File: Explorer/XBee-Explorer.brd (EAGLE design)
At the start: 35.6 x 27.9 mm, 31 parts, among them U2 XBEE-1B3, U3 MIC5205 3.3V, U4 FT231XS, X1 USBSMD

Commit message: Added jumper to disconnect RSSI LED, moved silk
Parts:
- removed U$2: CREATIVE_COMMONS, SparkFun:CREATIVE_COMMONS
- added FRAME1: FRAME-LETTER, SparkFun-Aesthetics:CREATIVE_COMMONS
- added LOGO1: OSHW-LOGOS, SparkFun-Aesthetics:OSHW-LOGO-S
- added SJ1: RSSI_LED_EN, SparkFun-Passives:SJ_2S-TRACE
- JP5, JP6: value M11PTH -> M111X11_NO_SILK; device SparkFun-Connectors:1X11 -> SparkFun-Connectors:1X11_NO_SILK
- moved JP4 1.80 mm to (3.81, 26.7)
- moved JP1 0.36 mm to (31.8, 1.27)
- moved U$1 0.13 mm to (4.70, 1.27)
- turned LED2 to 180 degrees
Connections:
- new net N$9: R7.2, SJ1.2
- net RSSI: now also SJ1.1; no longer R7.2
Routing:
- net N$9: track 0.00 -> 5.75 mm, vias 0 -> 1
- net TXLED: track 19.5 -> 20.3 mm
- net N$1: track 6.66 -> 7.28 mm
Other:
- board text added: "Nathan Seidle, Jim Lindblom"
- board text added: "RSSI LED"
- board text added: "v21"
- board text removed: "v20"
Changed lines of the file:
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@@
 <?xml version="1.0" encoding="utf-8"?>
 <!DOCTYPE eagle SYSTEM "eagle.dtd">
-<eagle version="6.4">
+<eagle version="6.5.0">
 <drawing>
 <settings>
@@
 <layer number="106" name="bPlate" color="7" fill="1" visible="no" active="yes"/>
 <layer number="107" name="Crop" color="7" fill="1" visible="no" active="yes"/>
+<layer number="108" name="tplace-old" color="10" fill="1" visible="no" active="yes"/>
+<layer number="109" name="ref-old" color="11" fill="1" visible="no" active="yes"/>
 <layer number="116" name="Patch_BOT" color="9" fill="4" visible="no" active="yes"/>
 <layer number="121" name="_tsilk" color="7" fill="1" visible="no" active="yes"/>
@@
 <wire x1="27.686" y1="1.778" x2="33.401" y2="8.382" width="0.254" layer="21"/>
 <wire x1="27.686" y1="26.162" x2="33.401" y2="19.558" width="0.254" layer="21"/>
-<text x="0.762" y="21.082" size="1.016" layer="21" ratio="15">PWR</text>
-<text x="31.796" y="13.413" size="1.016" layer="21" ratio="15">TX</text>
-<text x="31.877" y="9.652" size="1.016" layer="21" ratio="15">RX</text>
-<text x="1.27" y="12.446" size="1.27" layer="16" ratio="20" rot="MR90">v20</text>
-<text x="30.353" y="17.272" size="1.016" layer="21" ratio="15">RSSI</text>
+<text x="2.54" y="21.082" size="1.016" layer="21" ratio="15" align="bottom-center">PWR</text>
+<text x="33.655" y="13.97" size="1.016" layer="21" ratio="15" align="center-right">TX</text>
+<text x="33.655" y="10.16" size="1.016" layer="21" ratio="15" align="center-right">RX</text>
+<text x="1.27" y="12.446" size="1.27" layer="16" ratio="20" rot="MR90">v21</text>
+<text x="33.655" y="17.78" size="1.016" layer="21" ratio="15" align="center-right">RSSI</text>
 <text x="28.448" y="20.066" size="1.016" layer="22" ratio="15" rot="MR270">3.3V</text>
 <text x="25.908" y="20.066" size="1.016" layer="22" ratio="15" rot="MR270">DOUT</text>
@@
 <text x="4.572" y="7.874" size="1.016" layer="22" ratio="15" rot="MR90">5V</text>
 <text x="30.988" y="20.066" size="1.016" layer="22" ratio="15" rot="MR270">GND</text>
-<text x="21.59" y="-7.62" size="1.778" layer="21" font="vector" ratio="15">N. Seidle</text>
+<text x="21.59" y="-7.62" size="1.778" layer="27" font="vector" ratio="15">N. Seidle</text>
+<wire x1="14.732" y1="24.13" x2="15.748" y2="24.13" width="0.4064" layer="30"/>
+<text x="15.24" y="25.908" size="0.889" layer="22" ratio="15" rot="MR0" align="center">RSSI LED</text>
+<text x="17.78" y="-10.16" size="1.778" layer="51" font="vector">Nathan Seidle, Jim Lindblom</text>
 </plain>
 <attributes>
@@
 <attribute name="VALUE" x="3.937" y="19.6215" size="0.4064" layer="27"/>
 </element>
-<element name="LED2" library="SparkFun" package="LED-0603" value="Red-TX" x="34.29" y="13.97" smashed="yes">
-<attribute name="NAME" x="34.29" y="11.97" size="1.27" layer="25" rot="R270"/>
-<attribute name="VALUE" x="34.925" y="13.398" size="0.4064" layer="27" rot="R270"/>
+<element name="LED2" library="SparkFun" package="LED-0603" value="Red-TX" x="34.29" y="13.97" smashed="yes" rot="R180">
+<attribute name="NAME" x="34.29" y="15.97" size="1.27" layer="25" rot="R90"/>
+<attribute name="VALUE" x="33.655" y="14.542" size="0.4064" layer="27" rot="R90"/>
 </element>
 <element name="LED3" library="SparkFun" package="LED-0603" value="Green-RX" x="34.29" y="10.16" smashed="yes" rot="R180">
@@
 <attribute name="VALUE" x="33.528" y="10.732" size="0.4064" layer="27" rot="R90"/>
 </element>
-<element name="U$1" library="SparkFun" package="SFE-LOGO-FLAME" value="LOGO-SFESK" x="4.826" y="1.27"/>
+<element name="U$1" library="SparkFun" package="SFE-LOGO-FLAME" value="LOGO-SFESK" x="4.699" y="1.27"/>
 <element name="U$4" library="SparkFun" package="SFE-NEW-WEBLOGO" value="LOGO-SFENEW" x="26.924" y="11.43" rot="MR0"/>
 <element name="U2" library="SparkFun" package="XBEE-SMD" value="XBEE-1B3" x="6.35" y="13.97" smashed="yes" rot="R270">
@@
 <element name="U3" library="SparkFun" package="SOT23-5" value="MIC5205 3.3V" x="27.94" y="17.78" rot="R270"/>
 <element name="C1" library="SparkFun" package="EIA3216" value="10uF" x="27.94" y="12.7"/>
-<element name="U$2" library="SparkFun" package="CREATIVE_COMMONS" value="CREATIVE_COMMONS" x="-10.16" y="-7.62"/>
-<element name="JP1" library="SparkFun" package="MICRO-FIDUCIAL" value="FIDUCIALUFIDUCIAL" x="31.496" y="1.016"/>
-<element name="JP4" library="SparkFun" package="MICRO-FIDUCIAL" value="FIDUCIALUFIDUCIAL" x="5.08" y="25.4"/>
+<element name="JP1" library="SparkFun" package="MICRO-FIDUCIAL" value="FIDUCIALUFIDUCIAL" x="31.75" y="1.27"/>
+<element name="JP4" library="SparkFun" package="MICRO-FIDUCIAL" value="FIDUCIALUFIDUCIAL" x="3.81" y="26.67"/>
 <element name="U4" library="SparkFun-DigitalIC" package="SSOP20_L" value="FT231XS" x="19.05" y="13.97" rot="R180"/>
 <element name="R2" library="SparkFun-Resistors" package="0603-RES" value="27" x="11.43" y="14.224"/>
@@
 <element name="C6" library="SparkFun-Capacitors" package="0603-CAP" value="0.1uF" x="15.24" y="8.89" rot="R180"/>
 <element name="C7" library="SparkFun-Capacitors" package="0603-CAP" value="0.1uF" x="27.94" y="15.24" rot="R180"/>
-<element name="JP5" library="SparkFun-Connectors" package="1X11" value="M11PTH" x="5.08" y="21.463"/>
-<element name="JP6" library="SparkFun-Connectors" package="1X11" value="M11PTH" x="30.48" y="6.477" rot="R180"/>
+<element name="JP5" library="SparkFun-Connectors" package="1X11_NO_SILK" value="M111X11_NO_SILK" x="5.08" y="21.463"/>
+<element name="JP6" library="SparkFun-Connectors" package="1X11_NO_SILK" value="M111X11_NO_SILK" x="30.48" y="6.477" rot="R180"/>
+<element name="SJ1" library="SparkFun-Passives" package="SJ_2S-TRACE" value="RSSI_LED_EN" x="15.24" y="24.13" rot="MR180"/>
+<element name="FRAME1" library="SparkFun-Aesthetics" package="CREATIVE_COMMONS" value="FRAME-LETTER" x="-12.7" y="-10.16"/>
+<element name="LOGO1" library="SparkFun-Aesthetics" package="OSHW-LOGO-S" value="OSHW-LOGOS" x="5.588" y="25.908" rot="R90"/>
 </elements>
 <signals>
@@
 <contactref element="LED2" pad="A"/>
 <contactref element="R4" pad="2"/>
-<wire x1="28.79" y1="10.414" x2="30.734" y2="10.414" width="0.254" layer="1"/>
-<wire x1="34.29" y1="13.22" x2="33.54" y2="13.22" width="0.254" layer="1"/>
-<wire x1="33.54" y1="13.22" x2="30.734" y2="10.414" width="0.254" layer="1"/>
+<wire x1="28.79" y1="10.414" x2="29.337" y2="10.414" width="0.254" layer="1"/>
+<wire x1="33.643" y1="14.72" x2="29.337" y2="10.414" width="0.254" layer="1"/>
+<wire x1="34.29" y1="14.72" x2="33.643" y2="14.72" width="0.254" layer="1"/>
 </signal>
 <signal name="N$4">
@@
 <contactref element="U4" pad="10"/>
 <via x="17.7165" y="15.3035" extent="1-16" drill="0.508"/>
-<wire x1="17.7165" y1="15.3035" x2="31.6865" y2="15.3035" width="0.254" layer="16"/>
+<wire x1="17.7165" y1="15.3035" x2="30.7975" y2="15.3035" width="0.254" layer="16"/>
 <wire x1="16.1925" y1="16.6497" x2="16.1925" y2="15.6845" width="0.254" layer="1"/>
 <wire x1="16.1925" y1="15.6845" x2="16.5735" y2="15.3035" width="0.254" layer="1"/>
 <wire x1="17.7165" y1="15.3035" x2="16.5735" y2="15.3035" width="0.254" layer="1"/>
-<wire x1="31.6865" y1="15.3035" x2="31.75" y2="15.24" width="0.254" layer="16"/>
-<via x="31.75" y="15.24" extent="1-16" drill="0.508"/>
-<wire x1="31.75" y1="15.24" x2="32.27" y2="14.72" width="0.254" layer="1"/>
-<wire x1="32.27" y1="14.72" x2="34.29" y2="14.72" width="0.254" layer="1"/>
+<wire x1="34.29" y1="13.22" x2="33.413" y2="13.22" width="0.254" layer="1"/>
+<wire x1="33.413" y1="13.22" x2="33.147" y2="12.954" width="0.254" layer="1"/>
+<via x="33.147" y="12.954" extent="1-16" drill="0.508"/>
+<wire x1="33.147" y1="12.954" x2="30.7975" y2="15.3035" width="0.254" layer="16"/>
 </signal>
 <signal name="DIO4">
@@
 <wire x1="10.35" y1="26.47" x2="10.35" y2="23.685" width="0.254" layer="1"/>
 <via x="21.6535" y="18.288" extent="1-16" drill="0.508"/>
-<wire x1="19.7485" y1="20.193" x2="8.89" y2="20.193" width="0.254" layer="16"/>
-<wire x1="8.89" y1="20.193" x2="7.62" y2="21.463" width="0.254" layer="16"/>
-<wire x1="19.7485" y1="20.193" x2="21.6535" y2="18.288" width="0.254" layer="16"/>
+<wire x1="10.033" y1="19.05" x2="7.62" y2="21.463" width="0.254" layer="16"/>
 <wire x1="21.9075" y1="16.6497" x2="21.9075" y2="18.034" width="0.254" layer="1"/>
 <wire x1="21.9075" y1="18.034" x2="21.6535" y2="18.288" width="0.254" layer="1"/>
 <contactref element="JP5" pad="2"/>
+<wire x1="21.6535" y1="18.288" x2="20.8915" y2="19.05" width="0.254" layer="16"/>
+<wire x1="20.8915" y1="19.05" x2="10.033" y2="19.05" width="0.254" layer="16"/>
 </signal>
 <signal name="RES1">
@@
 <signal name="RSSI">
 <contactref element="U2" pad="6"/>
-<contactref element="R7" pad="2"/>
-<wire x1="15.24" y1="20.193" x2="15.24" y2="21.463" width="0.254" layer="1"/>
 <wire x1="16.35" y1="23.47" x2="16.35" y2="22.573" width="0.254" layer="1"/>
 <wire x1="16.35" y1="22.573" x2="15.24" y2="21.463" width="0.254" layer="1"/>
-<wire x1="15.66" y1="19.05" x2="15.66" y2="19.773" width="0.254" layer="1"/>
-<wire x1="15.66" y1="19.773" x2="15.24" y2="20.193" width="0.254" layer="1"/>
 <contactref element="JP5" pad="5"/>
+<contactref element="SJ1" pad="1"/>
+<wire x1="14.732" y1="24.13" x2="14.732" y2="21.971" width="0.254" layer="16"/>
+<wire x1="14.732" y1="21.971" x2="15.24" y2="21.463" width="0.254" layer="16"/>
 </signal>
 <signal name="DIO12">
@@
 <wire x1="16.8275" y1="12.1285" x2="14.732" y2="14.224" width="0.254" layer="1"/>
 </signal>
+<signal name="N$9">
+<contactref element="R7" pad="2"/>
+<contactref element="SJ1" pad="2"/>
+<wire x1="15.66" y1="19.05" x2="15.66" y2="19.47" width="0.254" layer="1"/>
+<wire x1="15.66" y1="19.47" x2="16.51" y2="20.32" width="0.254" layer="1"/>
+<via x="16.51" y="20.32" extent="1-16" drill="0.508"/>
+<wire x1="16.51" y1="20.32" x2="16.51" y2="22.352" width="0.254" layer="16"/>
+<wire x1="16.51" y1="22.352" x2="15.748" y2="23.114" width="0.254" layer="16"/>
+<wire x1="15.748" y1="23.114" x2="15.748" y2="24.13" width="0.254" layer="16"/>
+</signal>
 </signals>
+<errors>
+</errors>
 </board>
 </drawing>

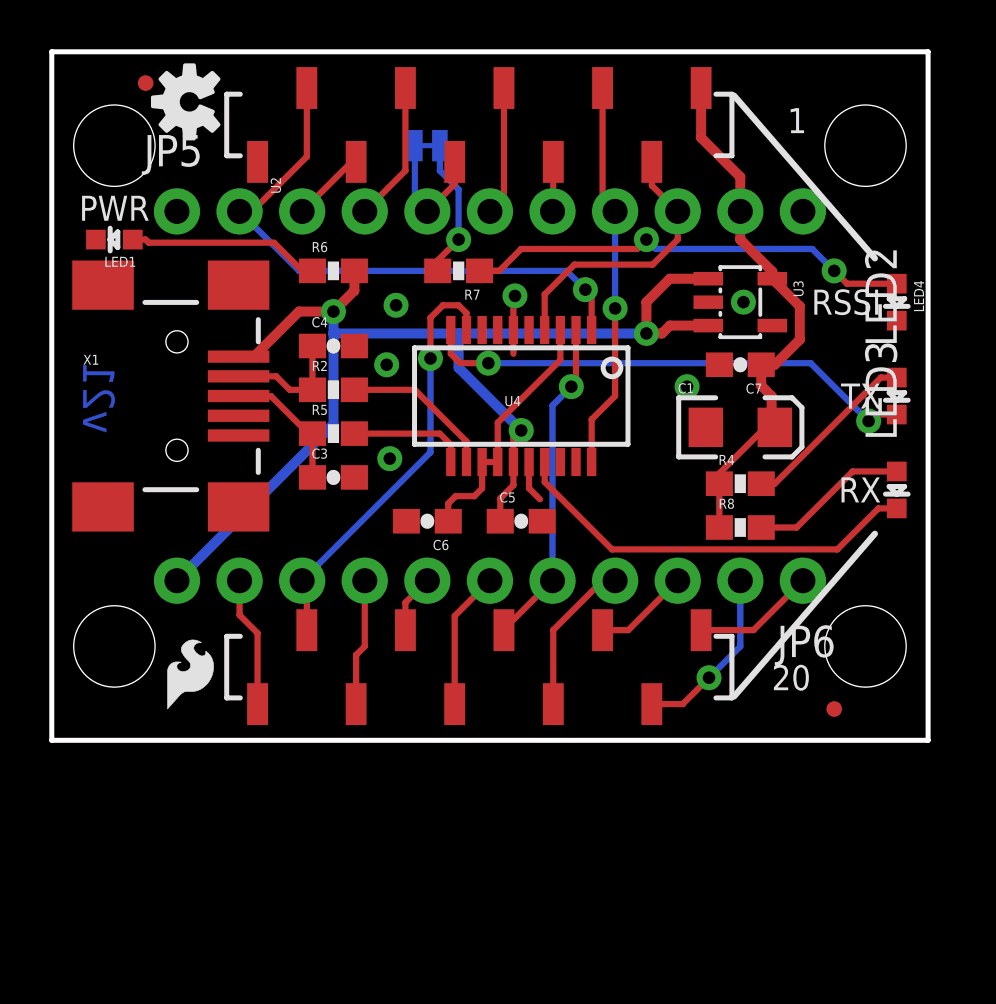
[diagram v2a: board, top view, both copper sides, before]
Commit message: Adding reset button, jumpers on UART ctrl lines
Reset button required moving LEDs around.
Adding jumpers on DTR, CTS, and RTS because they're not present on some
XBee compatible boards. Those pins can be used as GPIOs.
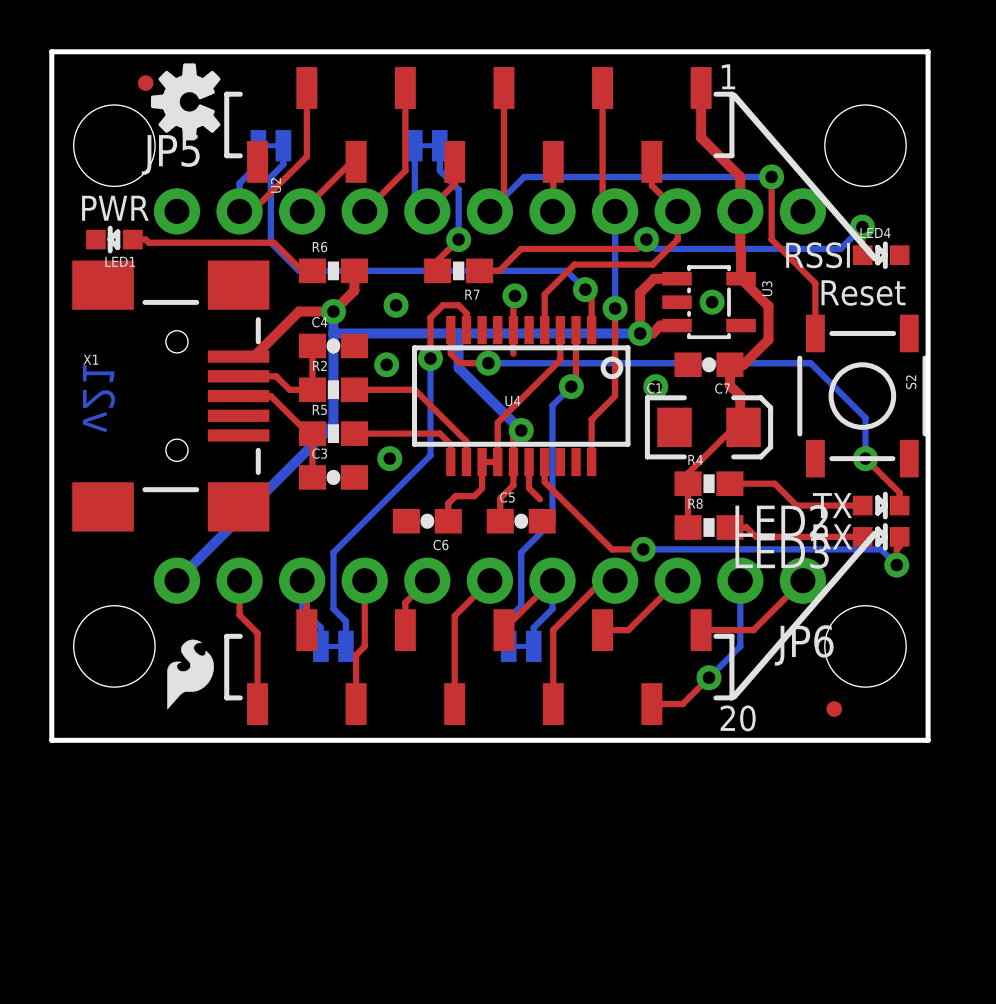
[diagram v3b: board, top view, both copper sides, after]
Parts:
- added S2: Reset, SparkFun-Electromechanical:TACTILE_SWITCH_SMD
- added SJ2: CTS_EN, SparkFun-Passives:SJ_2S-TRACE
- added SJ3: RTS_EN, SparkFun-Passives:SJ_2S-TRACE
- added SJ4: DTR, SparkFun-Passives:SJ_2S-TRACE
- moved LED2 4.49 mm to (33.7, 9.53), turned to 270 degrees
- moved LED3 2.01 mm to (33.7, 8.26), turned to 270 degrees
- moved LED4 2.01 mm to (33.7, 19.7), turned to 270 degrees
- moved C1 1.27 mm to (26.7, 12.7)
- moved C7 1.27 mm to (26.7, 15.2)
- moved R4 1.27 mm to (26.7, 10.4)
- moved R8 1.27 mm to (26.7, 8.64)
- moved U3 1.27 mm to (26.7, 17.8)
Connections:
- new net CTS_XBEE: JP6.9, SJ3.2, U2.12
- new net DTR_XBEE: JP5.2, SJ4.2, U2.9
- new net RTS_XBEE: JP6.5, SJ2.2, U2.16
- net CTS: now also SJ3.1; no longer JP6.9, U2.12
- net DTR: now also SJ4.1; no longer JP5.2, U2.9
- net GND: now also S2.1
- net RESET: now also S2.3
- net RTS: now also SJ2.1; no longer JP6.5, U2.16
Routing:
- net RESET: track 5.24 -> 24.3 mm, vias 0 -> 1
- net DTR_XBEE: track 0.00 -> 9.42 mm
- net RTS_XBEE: track 0.00 -> 5.81 mm
- net CTS_XBEE: track 0.00 -> 5.07 mm
- net DTR: track 23.5 -> 19.4 mm
- net TXLED: track 20.3 -> 23.0 mm
- net 5V: track 48.7 -> 46.6 mm
- net N$1: track 7.28 -> 5.75 mm
- net N$4: track 6.44 -> 5.54 mm
- net N$6: track 16.9 -> 17.7 mm, vias 0 -> 2
- net RTS: track 13.4 -> 14.0 mm
- net 3.3V: track 21.8 -> 21.3 mm
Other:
- board text added: "Reset"
- board text removed: "RSSI LED"

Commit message: Increasing fiducial size and LED footprint
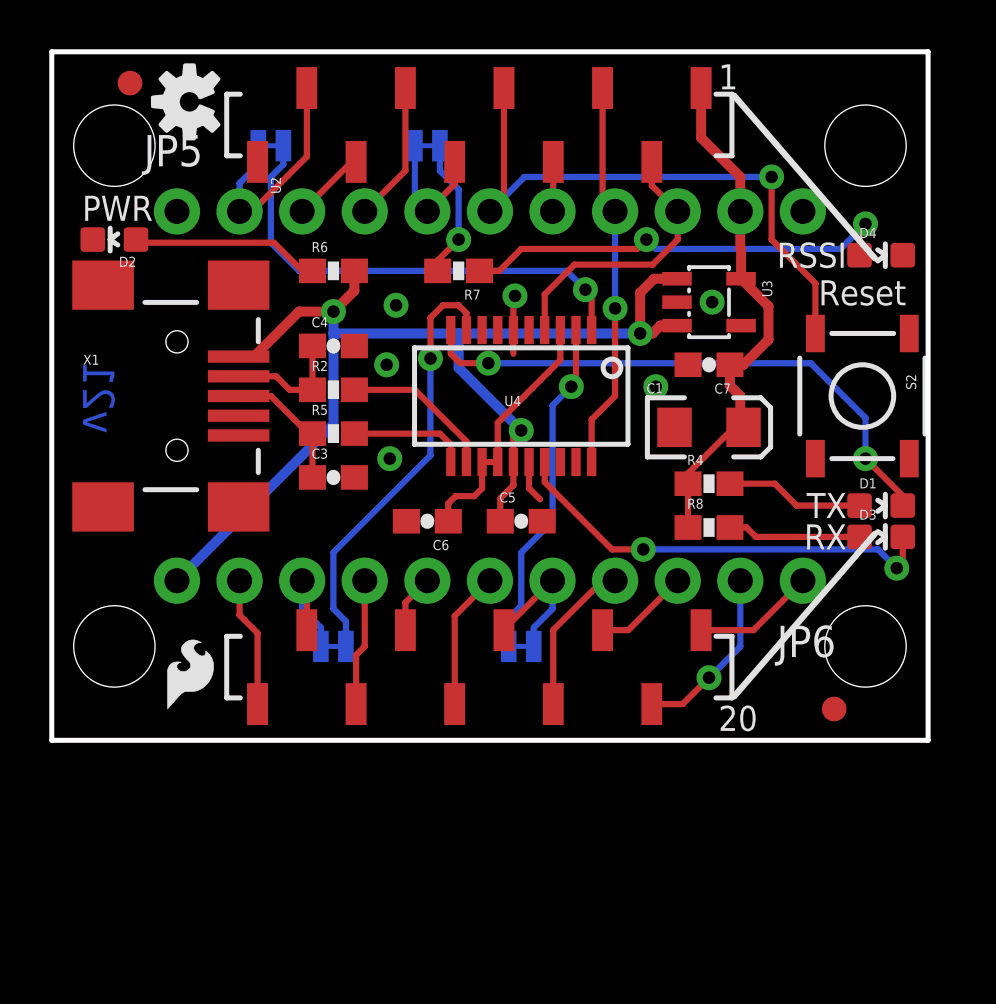
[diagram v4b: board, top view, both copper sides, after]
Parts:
- removed LED1: Red, SparkFun:LED-0603
- removed LED2: Red-TX, SparkFun:LED-0603
- removed LED3: Green-RX, SparkFun:LED-0603
- removed LED4: Green, SparkFun:LED-0603
- added D1, D2: RED, SparkFun-LED:LED-0603
- added D3, D4: GREEN, SparkFun-LED:LED-0603
- JP1, JP4: value FIDUCIALUFIDUCIAL -> FIDUCIAL1X2; device SparkFun:MICRO-FIDUCIAL -> SparkFun:FIDUCIAL-1X2
- moved JP4 0.64 mm to (3.17, 26.7)
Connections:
- net GND: now also D2.C, D4.C; no longer LED1.C, LED4.C
- net N$1: now also D1.A; no longer LED2.A
- net N$2: now also D4.A; no longer LED4.A
- net N$38: now also D2.A; no longer LED1.A
- net N$4: now also D3.A; no longer LED3.A
- net N$6: now also D3.C; no longer LED3.C
- net TXLED: now also D1.C; no longer LED2.C

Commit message: Updating VREG part info on explorer
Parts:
- U3: value MIC5205 3.3V -> MIC5219 3.3V
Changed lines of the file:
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@@
 <layer number="28" name="bValues" color="7" fill="1" visible="no" active="yes"/>
 <layer number="29" name="tStop" color="7" fill="3" visible="no" active="yes"/>
-<layer number="30" name="bStop" color="7" fill="6" visible="yes" active="yes"/>
+<layer number="30" name="bStop" color="7" fill="6" visible="no" active="yes"/>
 <layer number="31" name="tCream" color="7" fill="4" visible="no" active="yes"/>
 <layer number="32" name="bCream" color="7" fill="5" visible="no" active="yes"/>
@@
 <element name="U$10" library="SparkFun" package="STAND-OFF" value="STAND-OFF" x="33.02" y="24.13"/>
 <element name="U$11" library="SparkFun" package="STAND-OFF" value="STAND-OFF" x="33.02" y="3.81"/>
-<element name="U3" library="SparkFun" package="SOT23-5" value="MIC5205 3.3V" x="26.67" y="17.78" rot="R270"/>
+<element name="U3" library="SparkFun" package="SOT23-5" value="MIC5219 3.3V" x="26.67" y="17.78" rot="R270"/>
 <element name="C1" library="SparkFun" package="EIA3216" value="10uF" x="26.67" y="12.7"/>
 <element name="JP1" library="SparkFun" package="FIDUCIAL-1X2" value="FIDUCIAL1X2" x="31.75" y="1.27"/>
